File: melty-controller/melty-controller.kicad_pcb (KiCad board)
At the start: 4 copper layers, 43.5 x 15 mm, 33 parts, among them J1 Conn_01x02_Male, J2 soicbite, J3 esc_io, Q1 2N7002ET1G, U1 ESP32-PICO-D4, U2 AIC1734-33GUTR, U3 MMA1200KEG, U4 HT7250

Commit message: experiments and stuff
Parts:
- AE1: value Antenna_Chip -> AN9520-245
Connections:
- U2 pad 3: VBAT -> /V5.0
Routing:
- net /V5.0: track 12.8 -> 16.9 mm
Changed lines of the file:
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@@
     (thickness 1.6)
     (drawings 4)
-    (tracks 258)
+    (tracks 259)
     (modules 33)
     (nets 68)
@@
       (effects (font (size 1 1) (thickness 0.15)))
     )
-    (fp_text value "Antenna_Chip" (at 0 2.05 -90) (layer "F.Fab")
+    (fp_text value " AN9520-245 " (at 0 2.05 -90) (layer "F.Fab")
       (effects (font (size 1 1) (thickness 0.15)))
     )
@@
     )
     (pad "3" smd rect (at 1 0 90) (size 0.9 0.8) (layers "F.Cu" "F.Paste" "F.Mask")
-      (net 3 "VBAT") (pinfunction "VI"))
+      (net 33 "/V5.0") (pinfunction "VI"))
     (pad "2" smd rect (at -1 0.95 90) (size 0.9 0.8) (layers "F.Cu" "F.Paste" "F.Mask")
       (net 2 "VLOGIC") (pinfunction "VO"))
@@
   )
   (gr_rect (start 87 82.5) (end 130.5 97.5) (layer "Edge.Cuts") (width 0.1))
+  (segment (start 94.5 89.05) (end 94.5 85) (width 0.3) (layer "F.Cu") (net 33))
+  (segment (start 89 84.9) (end 89 86.5) (width 0.3) (layer "F.Cu") (net 3))
+  (segment (start 89 86.5) (end 92.5 90) (width 0.3) (layer "F.Cu") (net 3))
+  (segment (start 92.487501 84.224999) (end 95.160001 84.224999) (width 0.25) (layer "F.Cu") (net 3))
+  (segment (start 95.160001 84.224999) (end 95.210003 84.275001) (width 0.25) (layer "F.Cu") (net 3))
+  (segment (start 91.5 85.2125) (end 92.487501 84.224999) (width 0.25) (layer "F.Cu") (net 3))
+  (segment (start 95.210003 84.275001) (end 99.137499 84.275001) (width 0.25) (layer "F.Cu") (net 3))
+  (segment (start 99.137499 84.275001) (end 99.9125 83.5) (width 0.25) (layer "F.Cu") (net 3))
   (segment (start 119.165 94.765) (end 118.9 94.5) (width 0.15) (layer "B.Cu") (net 7))
   (segment (start 119.165 96.35) (end 119.165 94.765) (width 0.15) (layer "B.Cu") (net 7))
@@
   (via (at 96.1 83.5) (size 0.8) (drill 0.4) (layers "F.Cu" "B.Cu") (net 47))
   (segment (start 96.1 83.5) (end 97.5125 83.5) (width 0.2) (layer "B.Cu") (net 47))
-  (segment (start 95.02501 84.47499) (end 98.93751 84.47499) (width 0.2) (layer "F.Cu") (net 3))
-  (segment (start 94.5 85) (end 95.02501 84.47499) (width 0.2) (layer "F.Cu") (net 3))
-  (segment (start 98.93751 84.47499) (end 99.9125 83.5) (width 0.2) (layer "F.Cu") (net 3))
   (segment (start 123.3 85.6) (end 122.3 85.6) (width 0.2) (layer "In2.Cu") (net 49))
   (segment (start 104.7 87.8) (end 102.1 90.4) (width 0.2) (layer "In2.Cu") (net 49))
@@
   (segment (start 94.5 89.05) (end 95.8375 89.05) (width 0.3) (layer "F.Cu") (net 33))
   (segment (start 95.8375 89.05) (end 96 89.2125) (width 0.3) (layer "F.Cu") (net 33))
-  (segment (start 89 84.9) (end 89 86.5) (width 0.3) (layer "F.Cu") (net 3))
-  (segment (start 89 86.5) (end 92.5 90) (width 0.3) (layer "F.Cu") (net 3))
   (via (at 92.7125 86.7875) (size 0.8) (drill 0.4) (layers "F.Cu" "B.Cu") (net 1))
   (segment (start 92.7125 86.7875) (end 93.3375 86.7875) (width 0.3) (layer "F.Cu") (net 1))
@@
   (segment (start 93.3375 86.7875) (end 93.55 87) (width 0.3) (layer "F.Cu") (net 1))
   (segment (start 91.5 87) (end 91.5 86.7875) (width 0.3) (layer "F.Cu") (net 1))
-  (segment (start 91.5 85.2125) (end 94.2875 85.2125) (width 0.3) (layer "F.Cu") (net 3))
-  (segment (start 94.2875 85.2125) (end 94.5 85) (width 0.3) (layer "F.Cu") (net 3))
   (segment (start 89 84.9) (end 91.1875 84.9) (width 0.3) (layer "F.Cu") (net 3))
   (segment (start 91.1875 84.9) (end 91.5 85.2125) (width 0.3) (layer "F.Cu") (net 3))

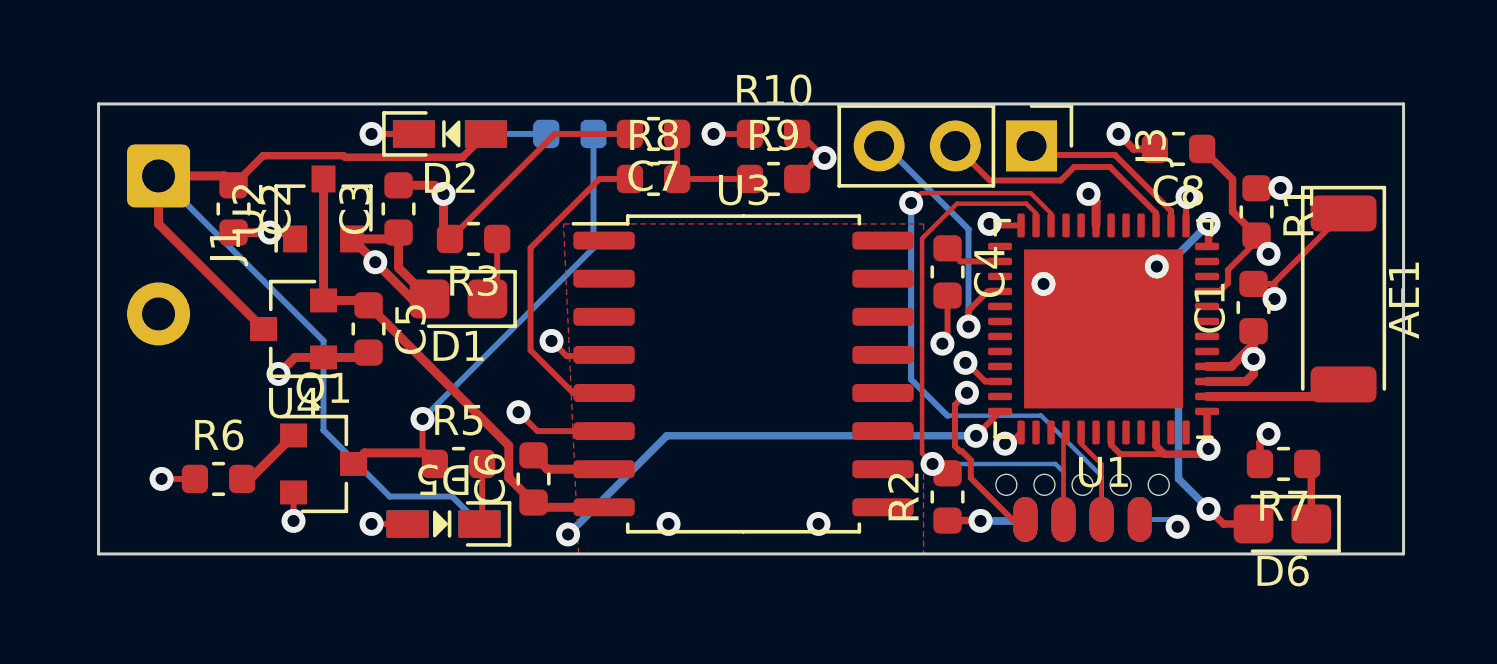
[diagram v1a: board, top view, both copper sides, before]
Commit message: switcharoo power to bigger dual ldo regulators
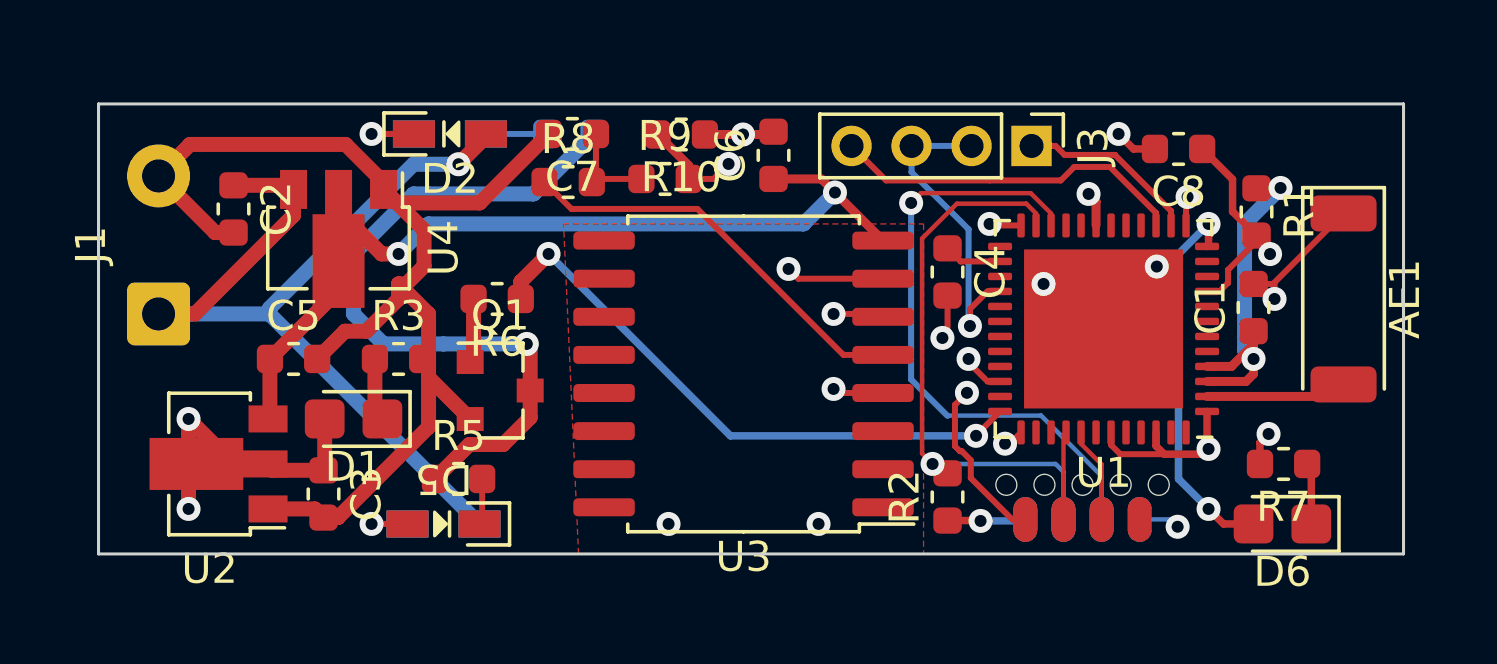
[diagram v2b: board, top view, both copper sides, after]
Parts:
- J3: footprint Connector_PinHeader_2.54mm:PinHeader_1x03_P2.54mm_Vertical -> Connector_PinHeader_2.00mm:PinHeader_1x04_P2.00mm_Vertical
- U2, U4: footprint Package_TO_SOT_SMD:SOT-23 -> Package_TO_SOT_SMD:SOT-89-3
- moved C6 13.4 mm to (109.5, 84.2)
- moved R6 11.1 mm to (100.3, 89.0), turned to 180 degrees
- moved C3 9.82 mm to (94.5, 95.5), turned to -90 degrees
- moved U2 9.19 mm to (91.0, 94.5), turned to 180 degrees
- moved Q1 6.38 mm to (100.4, 92.1)
- moved D1 5.32 mm to (95.5, 93.0)
- moved R3 4.72 mm to (97.0, 91.0), turned to 0 degrees
- moved J1 4.60 mm to (89.0, 89.5), turned to 90 degrees
- moved R9 3.62 mm to (105.9, 85.0)
- moved U4 3.35 mm to (95.0, 87.0), turned to -90 degrees
- moved R10 3.08 mm to (106.4, 83.5), turned to 180 degrees
- moved R8 2.85 mm to (102.7, 85.1)
- moved C7 2.71 mm to (102.8, 83.5)
- moved C5 2.69 mm to (93.5, 91.0), turned to 0 degrees
- moved R5 0.50 mm to (99.0, 95.0)
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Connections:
- J3 pad 2: /MOTOR2OUT -> /U1RXD
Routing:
- net GND: track 32.0 -> 57.3 mm, vias 14 -> 11
- net /V5.0: track 16.9 -> 31.7 mm, vias 0 -> 2
- net /ACCEL_STATUS: track 20.1 -> 8.24 mm
- net LED1: track 31.5 -> 19.8 mm, vias 3 -> 2
- net VLOGIC: track 24.3 -> 32.9 mm, vias 7 -> 8
- net Net-(Q1-Pad3): track 16.5 -> 24.4 mm
- net /ACCEL_SELF_TEST: track 26.1 -> 20.4 mm
- net /ACCEL_SENSE: track 9.93 -> 14.0 mm
- net /MOTOR2OUT: track 8.40 -> 12.2 mm
- net VBAT: track 35.6 -> 32.2 mm, vias 0 -> 1
- net /ACCEL_VOUT: track 10.7 -> 13.7 mm
- net /U1RXD: track 9.23 -> 10.6 mm
- net Net-(C7-Pad1): track 3.93 -> 3.36 mm
- net Net-(D5-Pad1): track 2.04 -> 1.54 mm

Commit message: clean up net names and stuff
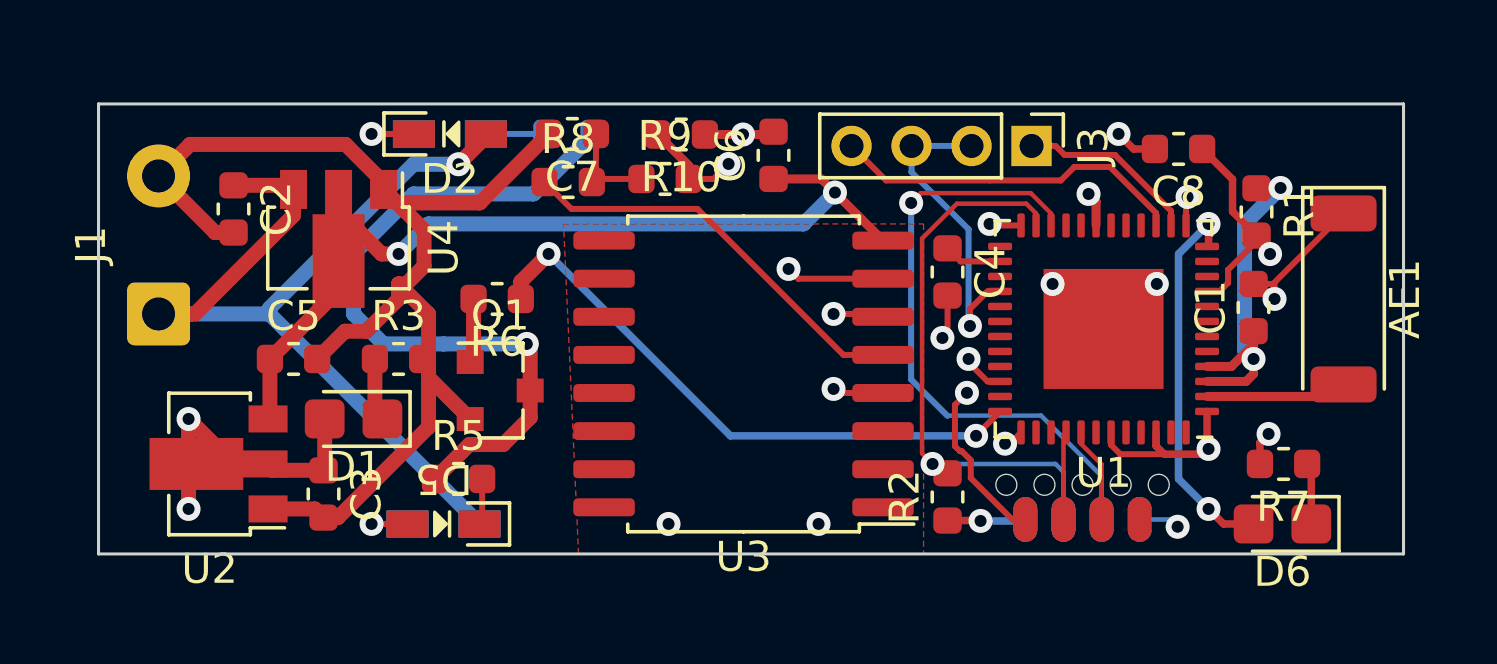
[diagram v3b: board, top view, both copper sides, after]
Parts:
- U1: footprint Package_DFN_QFN:QFN-48-1EP_7x7mm_P0.5mm_EP5.3x5.3mm -> melty-controller:esp32-pico-special
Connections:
- net ANT renamed /ANT
- net LED1 renamed /LED1
- net LED2 renamed /LED2
- net VBAT renamed /VBAT
- net VLOGIC renamed /VLOGIC

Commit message: Fix Antenna footprint; use zener to regulate 5.0v
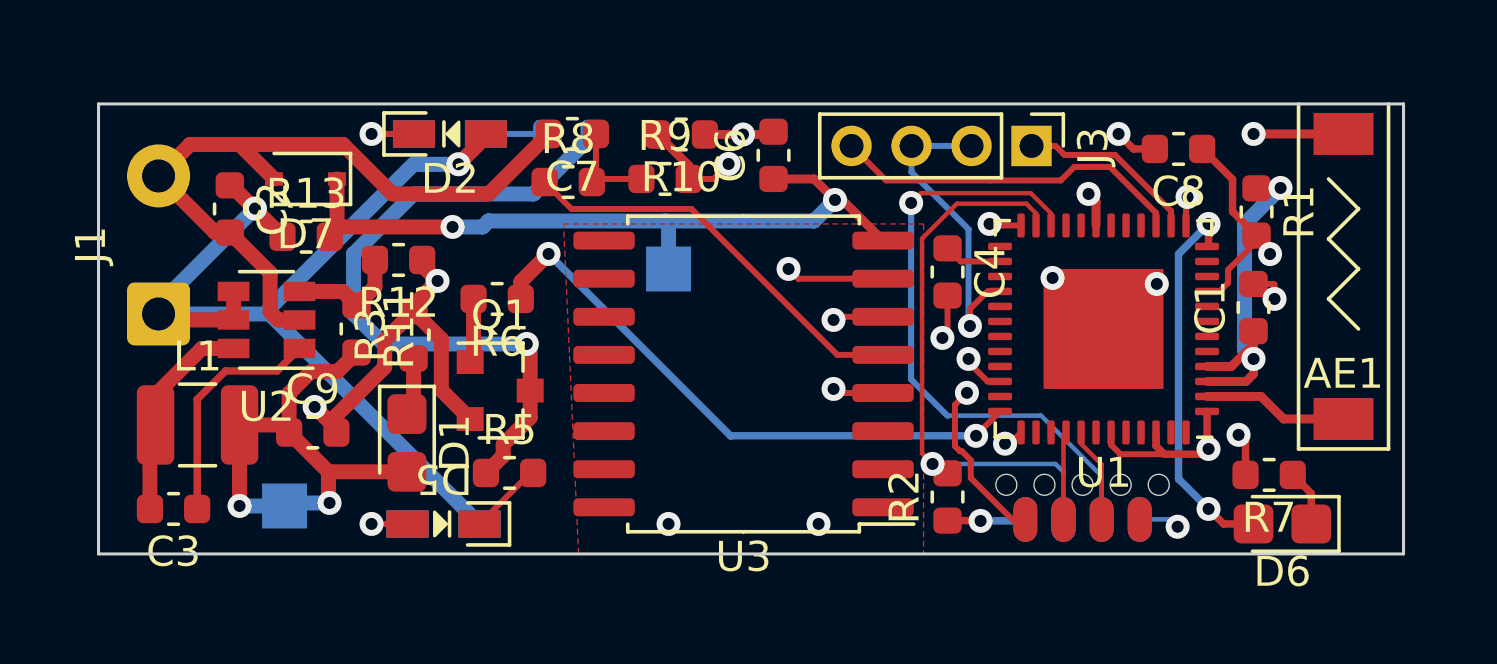
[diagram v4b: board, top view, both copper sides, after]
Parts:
- removed C5: 10uF, Capacitor_SMD:C_0603_1608Metric
- removed U4: HT7250, Package_TO_SOT_SMD:SOT-89-3
- added C9: 10uF, Capacitor_SMD:C_0603_1608Metric, F.Cu at (94.1, 93.5)
- added D7: 5.1v Zener, Diode_SMD:D_SOD-323, F.Cu at (93.9, 85.0)
- added L1: 10uH, Inductor_SMD:L_1210_3225Metric, F.Cu at (90.3, 93.2)
- added R11: 100k, Resistor_SMD:R_0603_1608Metric, F.Cu at (95.6, 90.0)
- added R12: 22k, Resistor_SMD:R_0603_1608Metric, F.Cu at (97.0, 87.7)
- added R13: 220R, Resistor_SMD:R_0603_1608Metric, F.Cu at (93.9, 86.9)
- added TP1: TestPoint, TestPoint:TestPoint_Pad_1.5x1.5mm, B.Cu at (93.2, 95.9)
- added TP2: TestPoint, TestPoint:TestPoint_Pad_1.5x1.5mm, B.Cu at (106.0, 88.0)
- AE1: footprint RF_Antenna:Johanson_2450AT43F0100 -> melty-controller:AN9520-245
- C3: value 10uF -> 22nF
- R1, R10, R2, R9: value 10k -> 22k
- U2: value AIC1734-33GUTR -> MT2492; footprint Package_TO_SOT_SMD:SOT-89-3 -> Package_TO_SOT_SMD:SOT-23-6
- moved U2 5.06 mm to (92.6, 89.7)
- moved C3 5.02 mm to (89.5, 96.0), turned to 180 degrees
- moved AE1 4.00 mm to (128.5, 93.0), turned to 0 degrees
- moved D1 1.95 mm to (97.3, 93.8), turned to -90 degrees
- moved R5 1.71 mm to (100.7, 94.8)
- moved R3 0.94 mm to (97.5, 90.2), turned to 90 degrees
- moved R7 0.60 mm to (126.0, 94.9)
- moved C2 0.12 mm to (91.4, 86.0)
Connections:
- AE1 pad 1: GND -> /ANT
- AE1 pad 2: /ANT -> GND
- C3 pad 1: /VLOGIC -> /REG_BS
- C3 pad 2: GND -> /REG_SW
- U2 pad 1: GND -> /REG_BS
- U2 pad 2: /VLOGIC -> GND
- U2 pad 3: /V5.0 -> /REG_FB
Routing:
- net /REG_BS: track 0.00 -> 7.77 mm
- net /VLOGIC: track 32.9 -> 40.1 mm
- net /REG_SW: track 0.00 -> 7.12 mm
- net /V5.0: track 31.7 -> 25.5 mm
- net /REG_FB: track 0.00 -> 3.86 mm
- net GND: track 57.3 -> 53.5 mm, vias 11 -> 14
- net /VBAT: track 32.2 -> 34.3 mm, vias 1 -> 2
- net Net-(Q1-Pad3): track 24.4 -> 22.8 mm
- net Net-(D5-Pad1): track 1.54 -> 2.49 mm

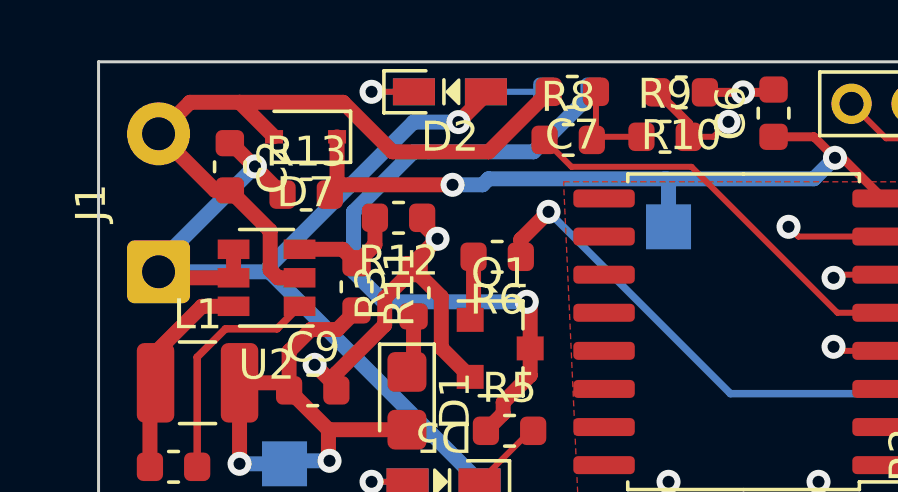
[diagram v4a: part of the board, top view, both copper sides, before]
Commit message: Use real regulator for 5.0 and tidy up schematic
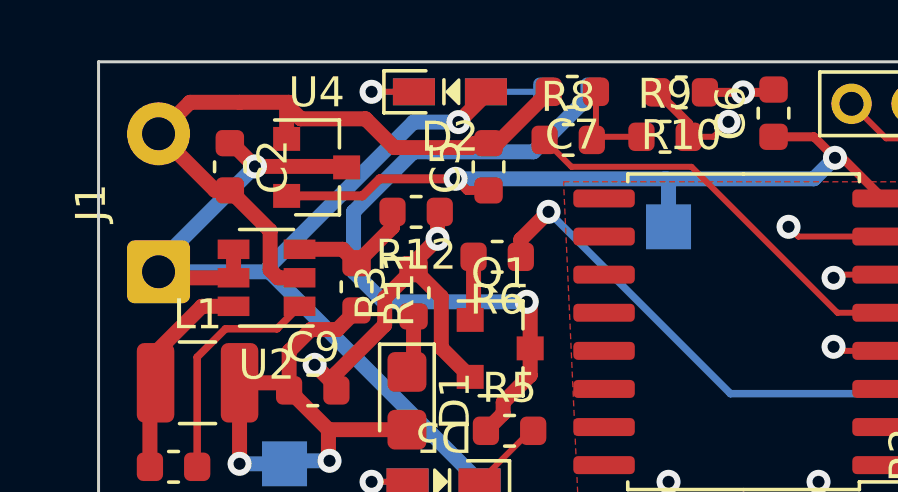
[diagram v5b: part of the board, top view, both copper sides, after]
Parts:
- removed D7: 5.1v Zener, Diode_SMD:D_SOD-323
- removed R13: 220R, Resistor_SMD:R_0603_1608Metric
- added C5: 10uF, Capacitor_SMD:C_0603_1608Metric, F.Cu at (100.0, 86.0)
- added U4: HT7250, Package_TO_SOT_SMD:SOT-23, F.Cu at (94.3, 86.0)
- moved R12 0.62 mm to (97.6, 87.5)
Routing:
- net /VBAT: track 34.3 -> 36.1 mm
- net /V5.0: track 25.5 -> 26.2 mm

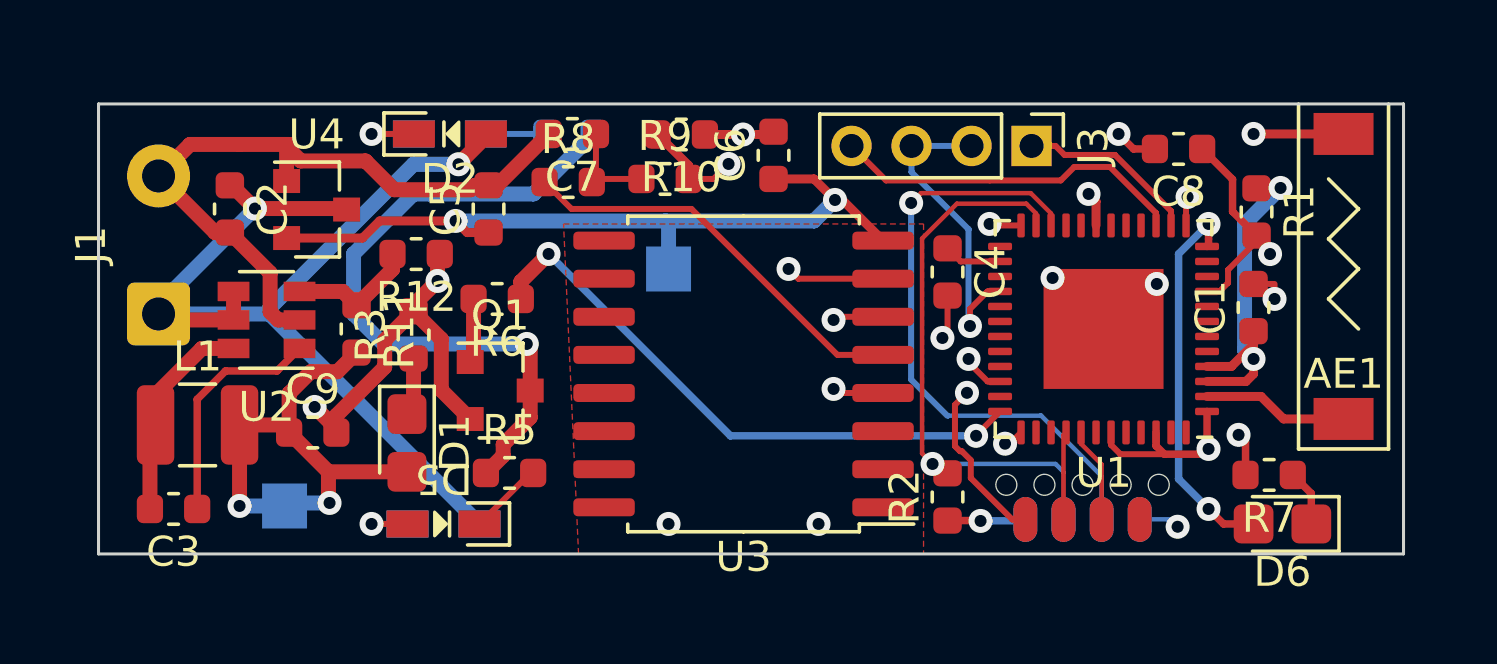
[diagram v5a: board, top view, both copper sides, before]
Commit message: Add more testpoints and minor fixes
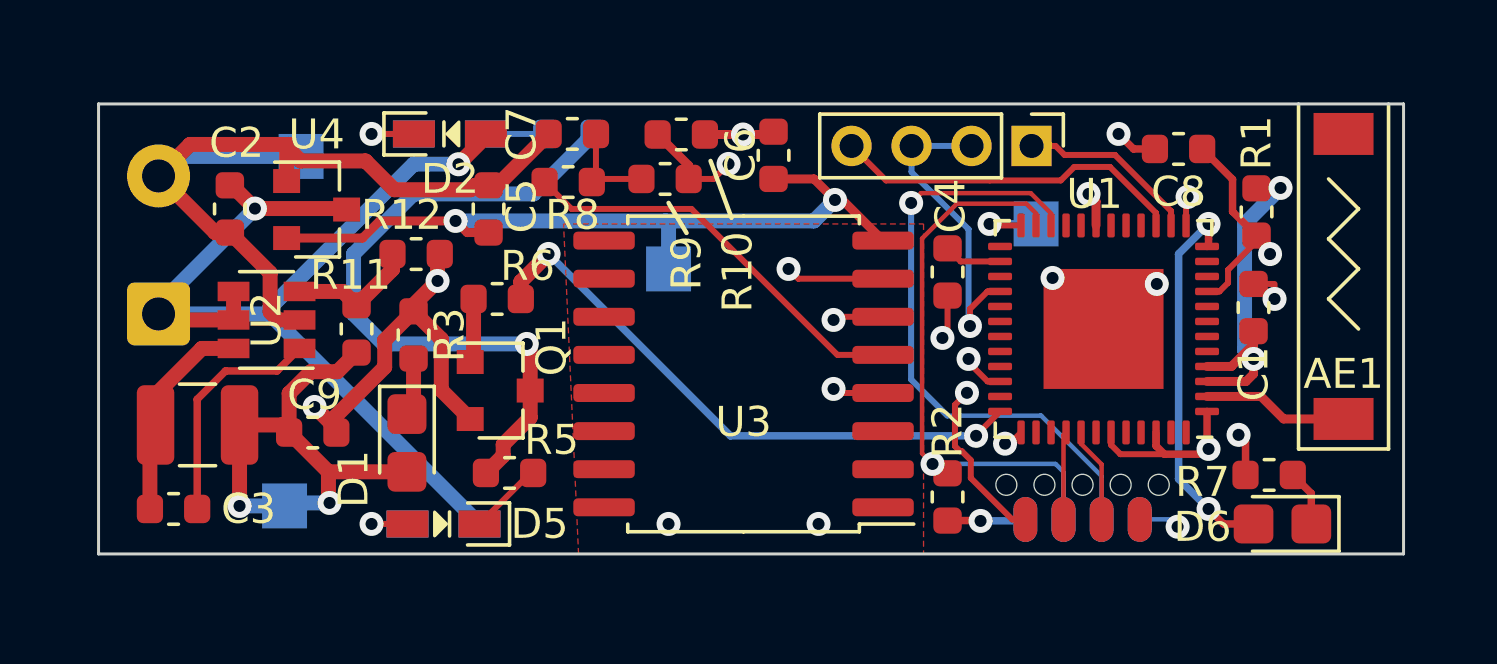
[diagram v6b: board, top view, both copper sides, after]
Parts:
- added TP3: TestPoint, TestPoint:TestPoint_Pad_1.5x1.5mm, B.Cu at (118.2, 86.5)
- added TP4: TestPoint, TestPoint:TestPoint_Pad_1.5x1.5mm, B.Cu at (93.8, 84.2)
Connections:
- AE1 pad 2: GND -> Net-(AE1-Pad2)
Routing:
- net GND: track 53.1 -> 55.1 mm, vias 14 -> 13
- net /ACCEL_SENSE: track 14.0 -> 15.6 mm
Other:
- board text added: "3.3v"
- board text added: "5v"
- board text added: "ACCEL"
- board text added: "GND"
